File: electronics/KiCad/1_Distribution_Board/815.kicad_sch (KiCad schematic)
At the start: 10 parts, among them J53 Conn_01x10, J54 Conn_01x06, J55 Signals 0-3, J56 Signals 4-7, J57 Module Left, J58 Conn_02x08_Odd_Even, J59 Module Right, J60 Signals 8-11, J61 Signals 12-15

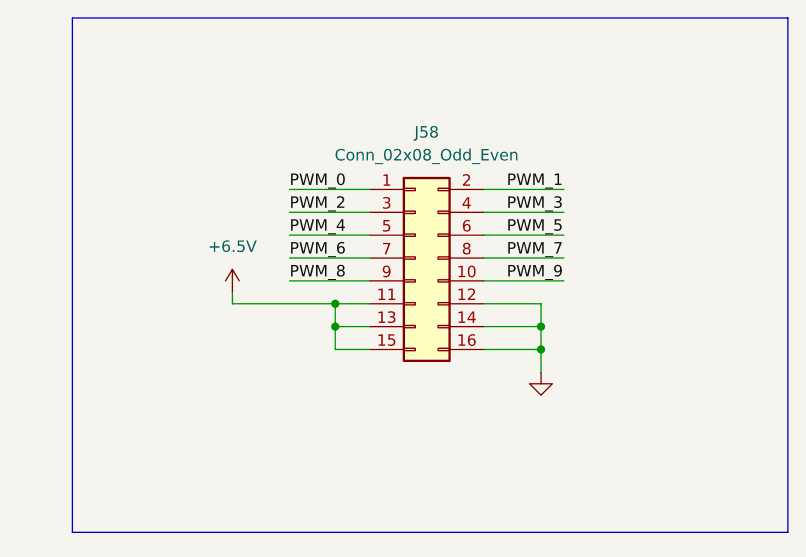
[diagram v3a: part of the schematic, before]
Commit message: Full Layout V0.1 Distributor
Full layout of distributor complete and ready for review. SCH updated but needs main page cleaned up.
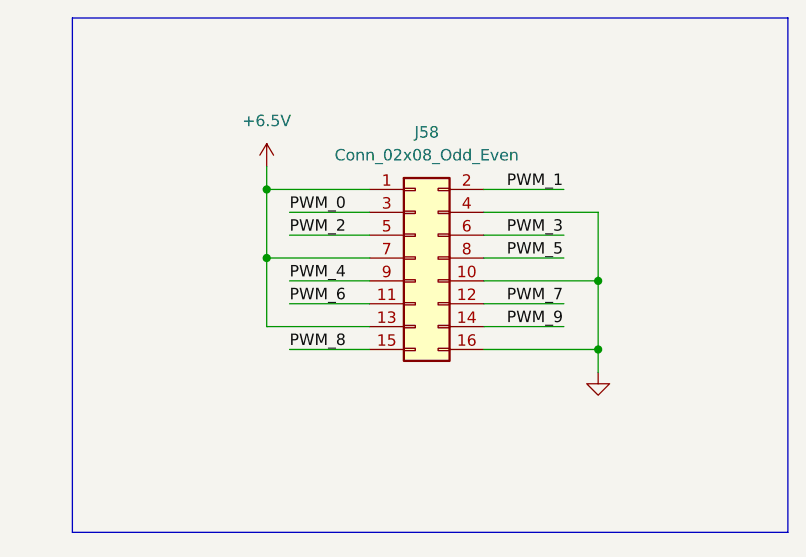
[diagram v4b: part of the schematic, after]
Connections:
- net +6.5V: now also J58.1 (Pin_1), J58.7 (Pin_7); no longer J58.11 (Pin_11), J58.15 (Pin_15)
- net GND: now also J58.10 (Pin_10), J58.4 (Pin_4); no longer J58.12 (Pin_12), J58.14 (Pin_14)
- net PWM_0: now also J58.3 (Pin_3); no longer J58.1 (Pin_1)
- net PWM_2: now also J58.5 (Pin_5); no longer J58.3 (Pin_3)
- net PWM_3: now also J58.6 (Pin_6); no longer J58.4 (Pin_4)
- net PWM_4: now also J58.9 (Pin_9); no longer J58.5 (Pin_5)
- net PWM_5: now also J58.8 (Pin_8); no longer J58.6 (Pin_6)
- net PWM_6: now also J58.11 (Pin_11); no longer J58.7 (Pin_7)
- net PWM_7: now also J58.12 (Pin_12); no longer J58.8 (Pin_8)
- net PWM_8: now also J58.15 (Pin_15); no longer J58.9 (Pin_9)
- net PWM_9: now also J58.14 (Pin_14); no longer J58.10 (Pin_10)

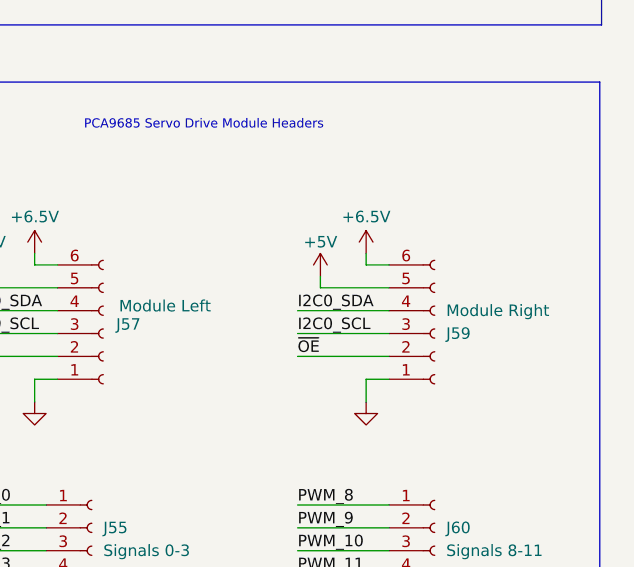
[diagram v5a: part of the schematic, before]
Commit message: Corrected net connections
Updated to connect GND on two resistors and eliminate the J59 netlist problem.
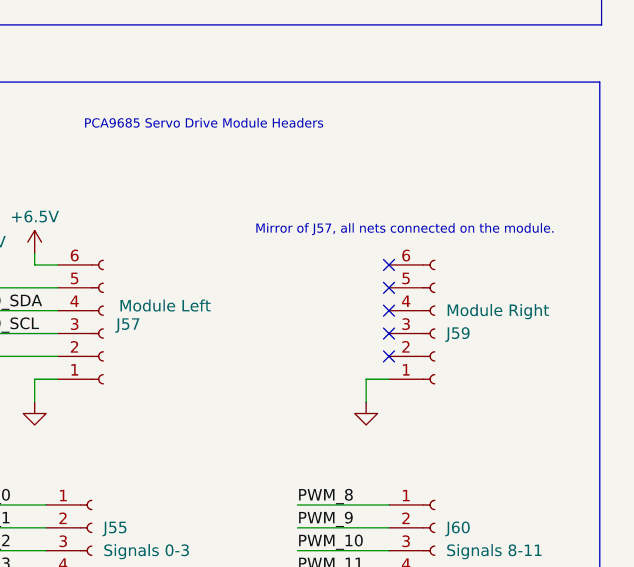
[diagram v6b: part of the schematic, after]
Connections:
- net +5V: no longer J59.5 (Pin_5)
- net +6.5V: no longer J59.6 (Pin_6)
- net I2C0_SCL: no longer J59.3 (Pin_3)
- net I2C0_SDA: no longer J59.4 (Pin_4)
- net ~{OE}: no longer J59.2 (Pin_2)
- no-connect marks 0 -> 5
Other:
- note added: "Mirror of J57, all nets connected on the module."
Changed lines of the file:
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@@
+		)
+	)
+	(text "Mirror of J57, all nets connected on the module."
+		(exclude_from_sim no)
+		(at 257.048 99.06 0)
+		(effects
+			(font
+				(size 1.016 1.016)
+			)
 		)
 	)
@@
 		(color 0 0 0 0)
 	)
+	(no_connect
+		(at 255.27 102.87)
+	)
+	(no_connect
+		(at 255.27 110.49)
+	)
+	(no_connect
+		(at 255.27 107.95)
+	)
+	(no_connect
+		(at 255.27 105.41)
+	)
+	(no_connect
+		(at 255.27 113.03)
+	)
 	(wire
 		(pts
@@
 	(wire
 		(pts
-			(xy 245.11 110.49) (xy 255.27 110.49)
-		)
-		(stroke
-			(width 0)
-			(type default)
-		)
-	)
-	(wire
-		(pts
 			(xy 127 106.68) (xy 127 105.41)
 		)
@@
 	(wire
 		(pts
-			(xy 255.27 105.41) (xy 247.65 105.41)
-		)
-		(stroke
-			(width 0)
-			(type default)
-		)
-	)
-	(wire
-		(pts
-			(xy 247.65 105.41) (xy 247.65 104.14)
-		)
-		(stroke
-			(width 0)
-			(type default)
-		)
-	)
-	(wire
-		(pts
 			(xy 220.98 45.72) (xy 220.98 38.1)
 		)
@@
 	(wire
 		(pts
-			(xy 245.11 113.03) (xy 255.27 113.03)
-		)
-		(stroke
-			(width 0)
-			(type default)
-		)
-	)
-	(wire
-		(pts
 			(xy 130.81 99.06) (xy 133.35 99.06)
 		)
@@
 	(wire
 		(pts
-			(xy 252.73 101.6) (xy 252.73 102.87)
-		)
-		(stroke
-			(width 0)
-			(type default)
-		)
-	)
-	(wire
-		(pts
 			(xy 255.27 132.08) (xy 245.11 132.08)
 		)
@@
 	(wire
 		(pts
-			(xy 252.73 102.87) (xy 255.27 102.87)
-		)
-		(stroke
-			(width 0)
-			(type default)
-		)
-	)
-	(wire
-		(pts
 			(xy 129.54 101.6) (xy 129.54 100.33)
 		)
@@
 		(pts
 			(xy 127 106.68) (xy 133.35 106.68)
-		)
-		(stroke
-			(width 0)
-			(type default)
-		)
-	)
-	(wire
-		(pts
-			(xy 245.11 107.95) (xy 255.27 107.95)
 		)
 		(stroke
@@
 		)
 	)
-	(label "~{OE}"
-		(at 245.11 113.03 0)
-		(effects
-			(font
-				(size 1.27 1.27)
-			)
-			(justify left bottom)
-		)
-	)
 	(label "PWM_3"
 		(at 207.01 137.16 0)
@@
 		)
 	)
-	(label "I2C0_SCL"
-		(at 245.11 110.49 0)
-		(effects
-			(font
-				(size 1.27 1.27)
-			)
-			(justify left bottom)
-		)
-	)
 	(label "PWM_5"
 		(at 207.01 146.05 0)
-		(effects
-			(font
-				(size 1.27 1.27)
-			)
-			(justify left bottom)
-		)
-	)
-	(label "I2C0_SDA"
-		(at 245.11 107.95 0)
 		(effects
 			(font
@@
 	)
 	(symbol
-		(lib_id "power:+5V")
-		(at 247.65 104.14 0)
-		(unit 1)
-		(exclude_from_sim no)
-		(in_bom yes)
-		(on_board yes)
-		(dnp no)
-		(property "Reference" "#PWR0138"
-			(at 247.65 107.95 0)
-			(effects
-				(font
-					(size 1.27 1.27)
-				)
-				(hide yes)
-			)
-		)
-		(property "Value" "+5V"
-			(at 247.65 100.33 0)
-			(effects
-				(font
-					(size 1.27 1.27)
-				)
-			)
-		)
-		(property "Footprint" ""
-			(at 247.65 104.14 0)
-			(effects
-				(font
-					(size 1.27 1.27)
-				)
-				(hide yes)
-			)
-		)
-		(property "Datasheet" ""
-			(at 247.65 104.14 0)
-			(effects
-				(font
-					(size 1.27 1.27)
-				)
-				(hide yes)
-			)
-		)
-		(property "Description" "Power symbol creates a global label with name \"+5V\""
-			(at 247.65 104.14 0)
-			(effects
-				(font
-					(size 1.27 1.27)
-				)
-				(hide yes)
-			)
-		)
-		(pin "1"
-		)
-		(instances
-			(project "1_Distribution_Board"
-				(path "/d53c8c01-e754-4310-8a73-7d7c95e64cd3/4f60e607-b8a0-4b26-ada7-74dd2d095020"
-					(reference "#PWR0138")
-					(unit 1)
-				)
-			)
-		)
-	)
-	(symbol
 		(lib_id "Connector:Conn_01x04_Socket")
 		(at 260.35 132.08 0)
@@
 					(unit 1)
 				)
-			)
-		)
-	)
-	(symbol
-		(lib_id "power:+6V")
-		(at 252.73 101.6 0)
-		(unit 1)
-		(exclude_from_sim no)
-		(in_bom yes)
-		(on_board yes)
-		(dnp no)
-		(property "Reference" "#PWR0140"
-			(at 252.73 105.41 0)
-			(effects
-				(font
-					(size 1.27 1.27)
-				)
-				(hide yes)
-			)
-		)
-		(property "Value" "+6.5V"
-			(at 252.73 97.536 0)
-			(effects
-				(font
-					(size 1.27 1.27)
-				)
-			)
-		)
-		(property "Footprint" ""
-			(at 252.73 101.6 0)
-			(effects
-				(font
-					(size 1.27 1.27)
-				)
-				(hide yes)
-			)
-		)
-		(property "Datasheet" ""
-			(at 252.73 101.6 0)
-			(effects
-				(font
-					(size 1.27 1.27)
-				)
-				(hide yes)
-			)
-		)
-		(property "Description" "Power symbol creates a global label with name \"+6V\""
-			(at 252.73 101.6 0)
-			(effects
-				(font
-					(size 1.27 1.27)
-				)
-				(hide yes)
-			)
-		)
-		(pin "1"
-		)
-		(instances
-			(project "1_Distribution_Board"
-				(path "/d53c8c01-e754-4310-8a73-7d7c95e64cd3/4f60e607-b8a0-4b26-ada7-74dd2d095020"
-					(reference "#PWR0140")
-					(unit 1)
-				)
